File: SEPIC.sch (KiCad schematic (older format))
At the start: 23 parts, among them J1 Screw_Terminal_01x02, J3 Screw_Terminal_01x02, J4 Conn_01x04_Male, J5 Conn_01x02_Male, J6 Conn_01x03_Male, J7 Screw_Terminal_01x02, U1 AP2205, U2 XL6009, U3 MCP48FVB21

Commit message: Mostly done
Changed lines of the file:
@@
 	7000 2500 7000 3050
-Wire Wire Line
-	7000 3350 7000 3500
-Connection ~ 7000 3500
-Wire Wire Line
-	7000 3500 7200 3500
-Wire Wire Line
-	7000 3500 7000 3650
 Wire Wire Line
 	2250 2500 2650 2500
@@
 Connection ~ 5750 2500
 Wire Wire Line
-	5750 3100 6300 3100
-Connection ~ 6300 3100
-Wire Wire Line
 	6300 2500 7000 2500
 Connection ~ 6300 2500
@@
 	0    -1   -1   0
 $EndComp
+Wire Wire Line
+	7000 3350 7000 3500
+Connection ~ 7000 3500
+Wire Wire Line
+	7000 3500 7000 3650
+Wire Wire Line
+	7200 3500 7000 3500
+$Comp
+L power:GND #PWR?
+U 1 1 61BCAFA8
+P 5750 3100
+F 0 "#PWR?" H 5750 2850 50  0001 C CNN
+F 1 "GND" H 5755 2927 50  0000 C CNN
+F 2 "" H 5750 3100 50  0001 C CNN
+F 3 "" H 5750 3100 50  0001 C CNN
+	1    5750 3100
+	1    0    0    -1
+$EndComp
 $EndSCHEMATC

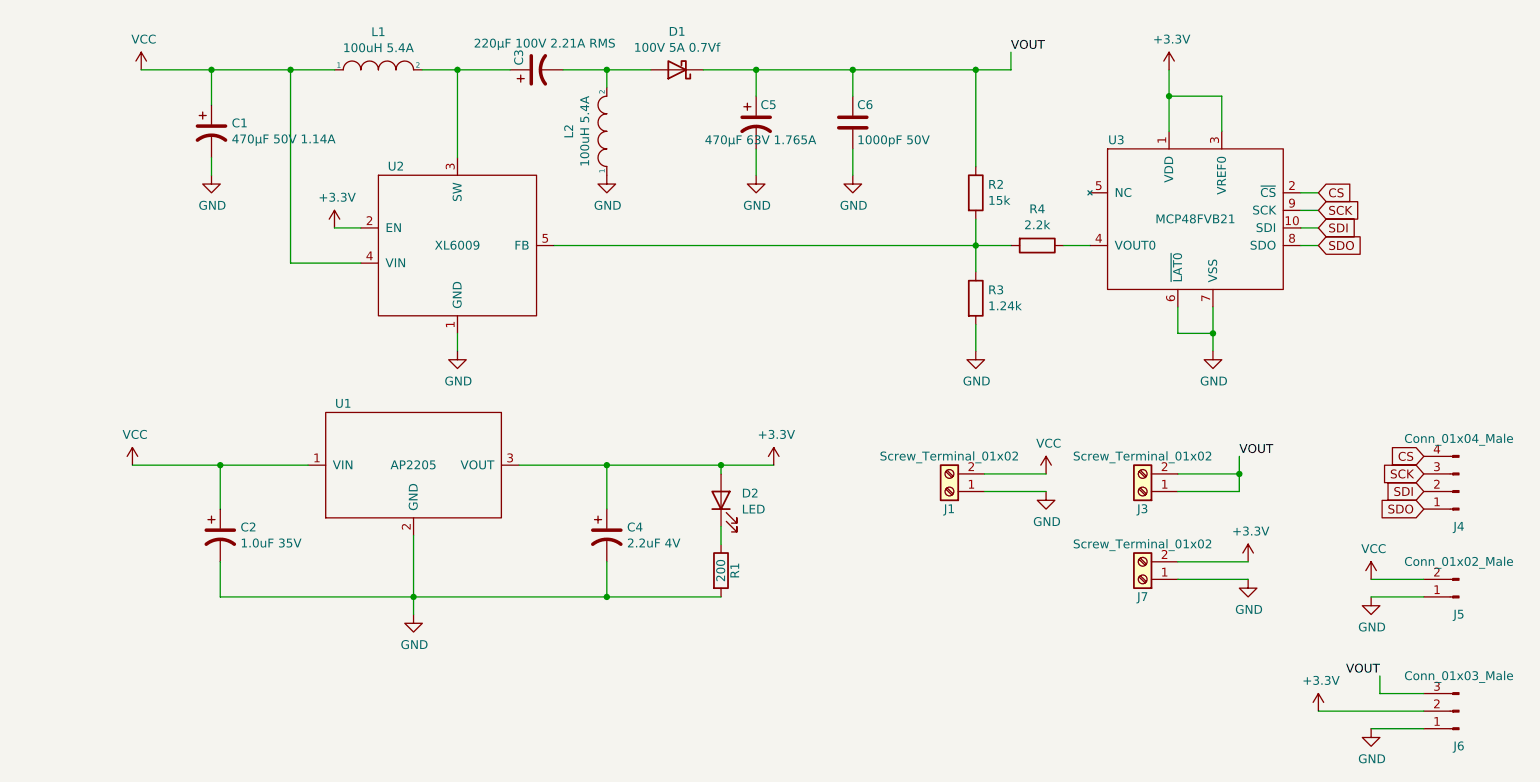
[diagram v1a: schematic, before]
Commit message: Added some optional capacitors
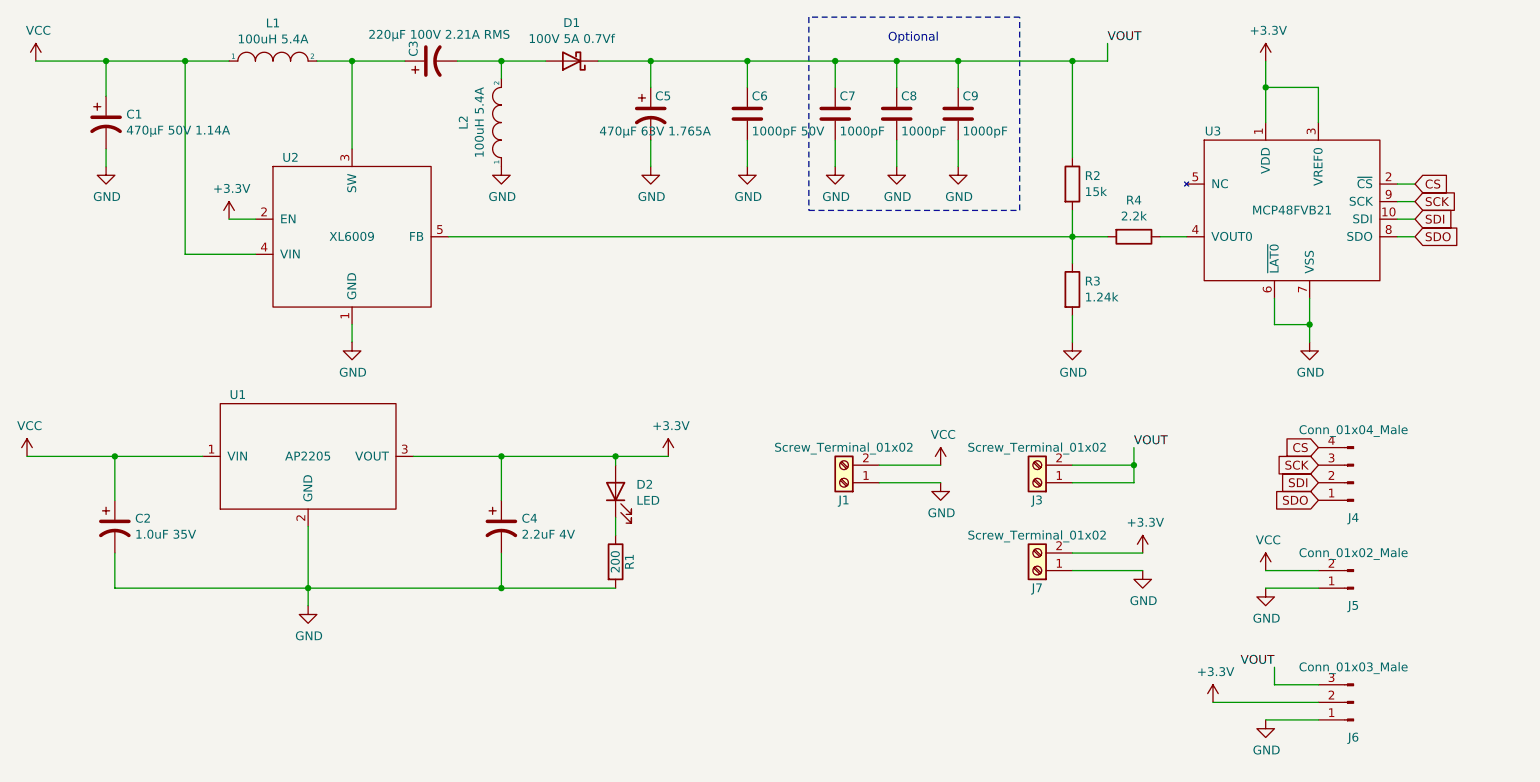
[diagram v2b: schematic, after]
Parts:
- added C7, C8, C9: 1000pF, Footprints:04025C102KAT2A, symbol Device:C
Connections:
- net GND: now also C7.2, C8.2, C9.2
- net VOUT: now also C7.1, C8.1, C9.1
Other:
- note added: "Optional"
- moved on the sheet: C1, C2, C3, C4, C5, C6, D1, D2, J1, J3, J4, J5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

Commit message: Added mounting hole
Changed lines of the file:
@@
 U 1 1 61CFEAB0
 P 3900 2450
-F 0 "C3" H 3925 2550 50  0000 L CNN
+F 0 "C3" V 3950 2500 50  0000 L CNN
 F 1 "220µF 100V 2.21A RMS" V 4050 2000 50  0000 L CNN
 F 2 "Footprints:100ZLJ220M12.5X25" H 3900 2450 50  0001 C CNN
